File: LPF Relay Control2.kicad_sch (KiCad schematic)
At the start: 12 parts, among them K11 EA2-5NU, K12 EA2-5NU, K13 EA2-5NU, K14 EA2-5NU, Q7 BSS123, Q8 BSS123

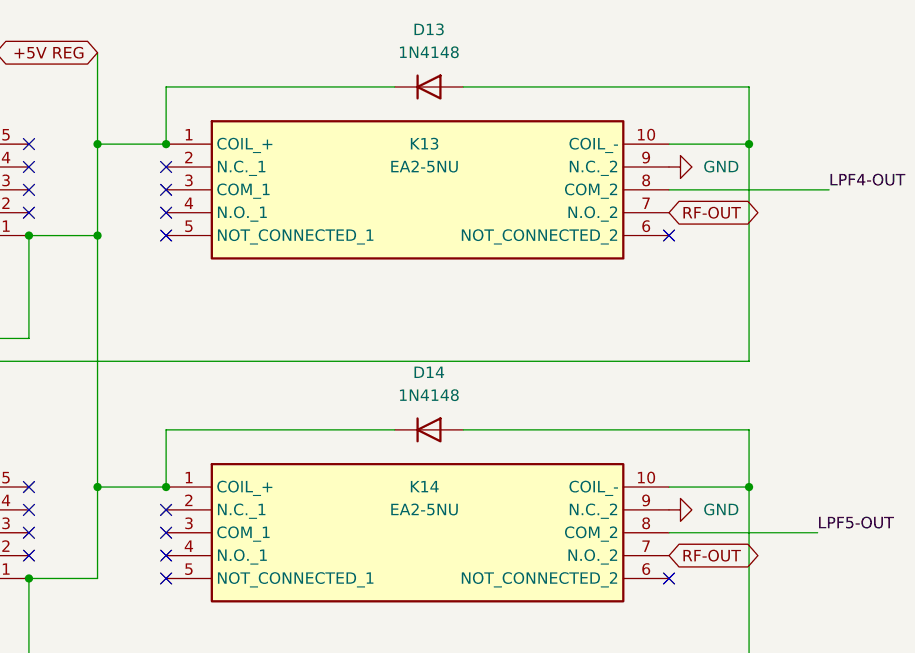
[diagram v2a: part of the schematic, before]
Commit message: Ron helped moved all the parts into PCB
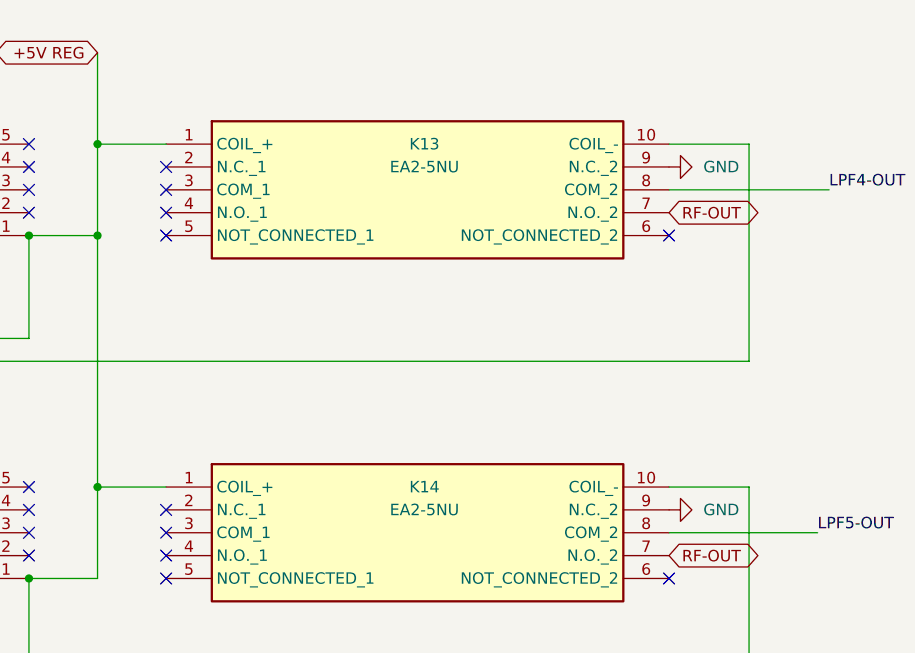
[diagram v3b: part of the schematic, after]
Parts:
- removed D13, D14: 1N4148, Diode_THT:D_DO-35_SOD27_P7.62mm_Horizontal, symbol Diode:1N4148
- R13, R14: footprint Resistor_THT:R_Axial_DIN0309_L9.0mm_D3.2mm_P12.70mm_Horizontal -> Resistor_SMD:R_0805_2012Metric_Pad1.20x1.40mm_HandSolder
